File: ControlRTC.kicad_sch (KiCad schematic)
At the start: 36 parts, among them M1 Fan_4pin, SW1 SW_USER, SW2 SW_WIPE, U18 74LVC1G07, U19 74LVC1G07, U20 LP5569RTWR, U21 PCF85063AT, U25 PCF8563TS, Y2 X32K768S301

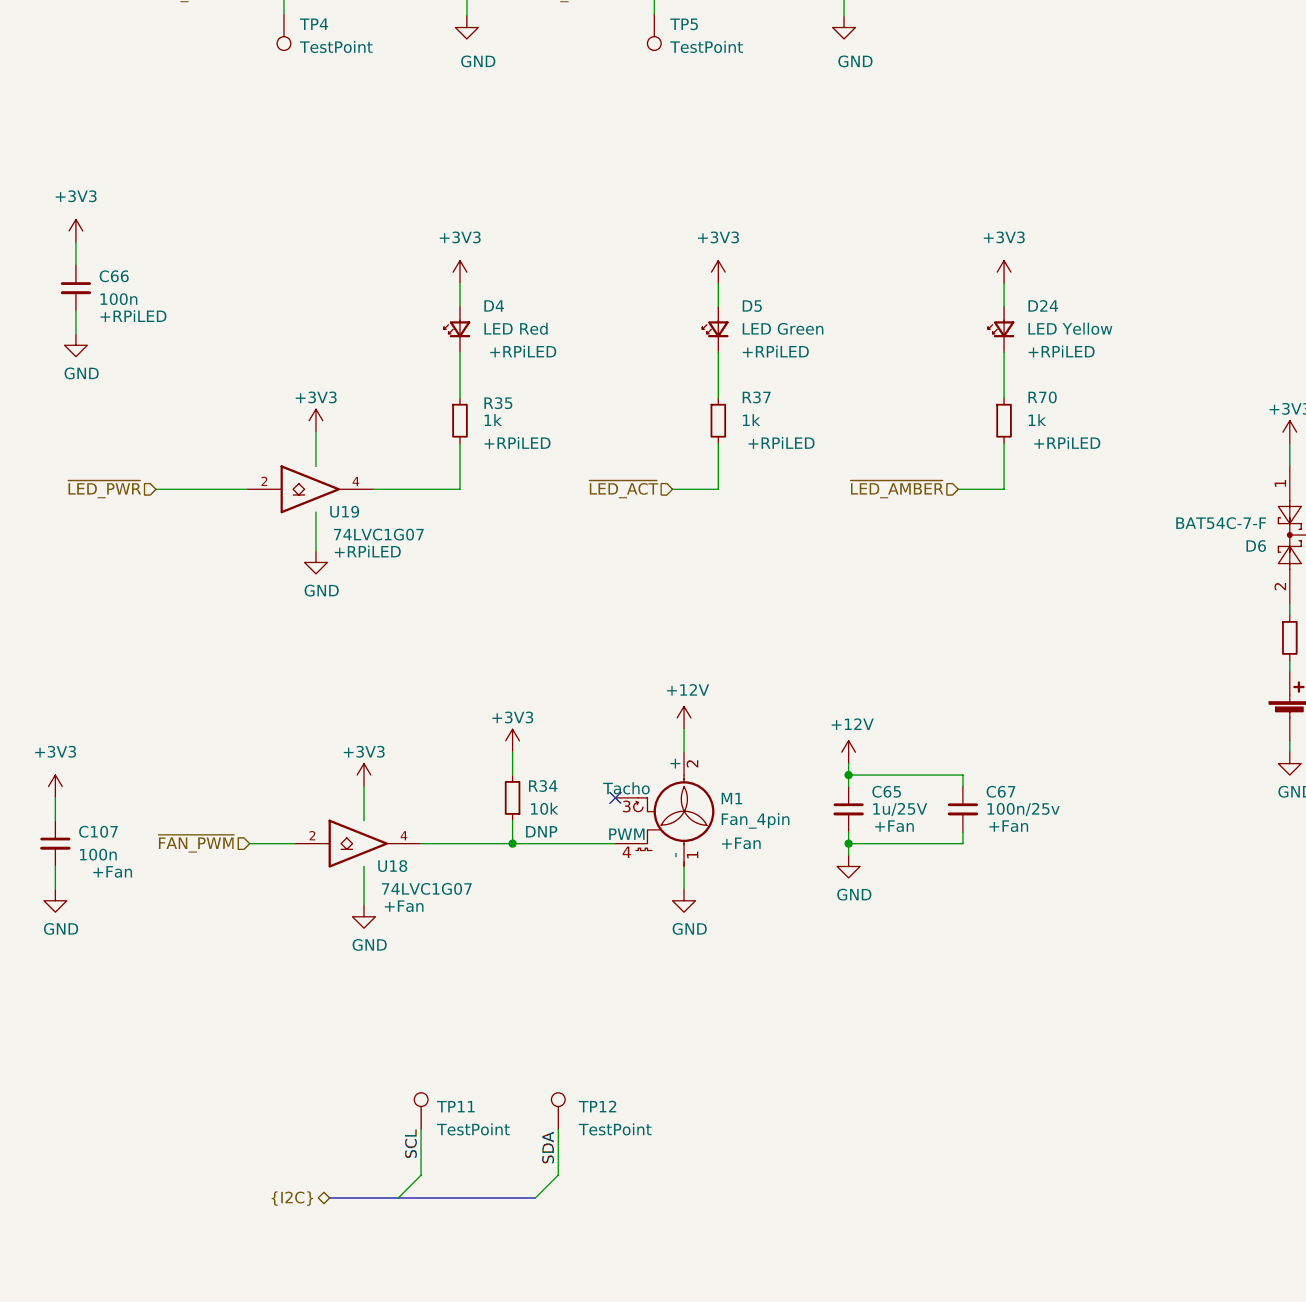
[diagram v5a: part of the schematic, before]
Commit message: Update to LEDs and add GND test point
- Add Blue Radio LED (in a separate new assembly option)
- Change buffer package from SC-70 to SC-74A (aka. SOT-23-5)
- Add GND test point

Fixes: #31

Signed-off-by: Stefan Agner <stefan@agner.ch>
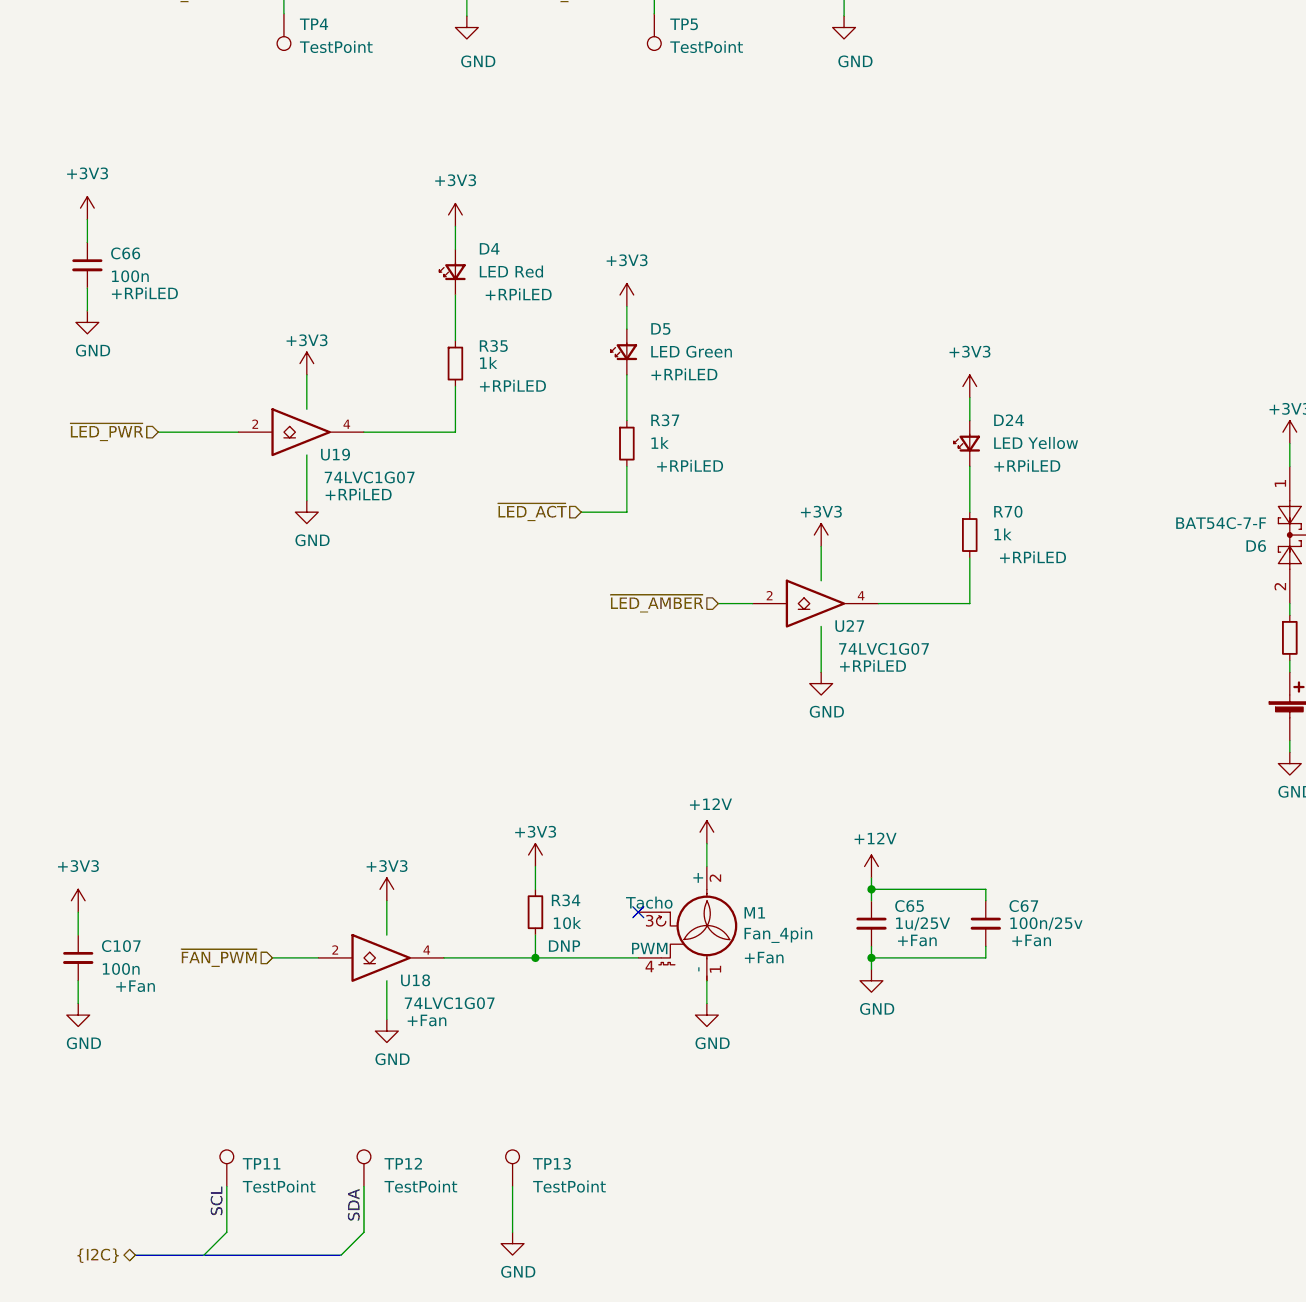
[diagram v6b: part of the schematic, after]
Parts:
- added TP13: TestPoint, TestPoint:TestPoint_Pad_D1.0mm, symbol Connector:TestPoint
- added U27: 74LVC1G07, Package_TO_SOT_SMD:SOT-23-5, symbol 74xGxx:74LVC1G07
- U18, U19: footprint Package_TO_SOT_SMD:SOT-353_SC-70-5 -> Package_TO_SOT_SMD:SOT-23-5; Manufacturer NXP USA -> Texas Instruments; PartNumber 74LVC1G07GW -> SN74LVC1G07DBV
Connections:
- net +3V3: now also U27.5 (VCC)
- net GND: now also TP13.1, U27.3 (GND)
- net ~{LED_AMBER}: now also U27.2; no longer R70.2
- new net: R70.2, U27.4
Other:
- moved on the sheet: C107, C65, C66, C67, D24, D4, D5, M1, R34, R35, R37, R70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

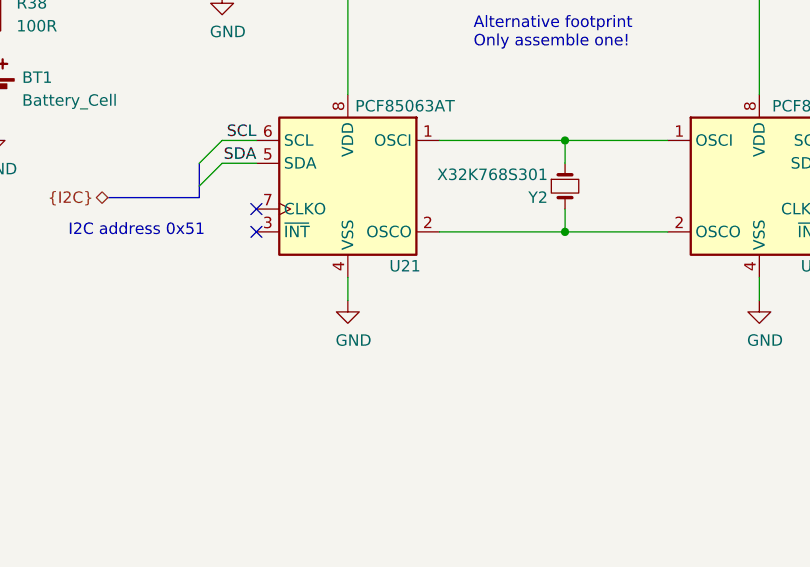
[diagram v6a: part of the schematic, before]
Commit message: Relayout new design
- Update PCB from Schematics
- Move SD-card to bottom side of the PCB
- Place LEDs in front of CM4
- Add additional LEDs (Amber/Radio)
- Move LP5569 to the left
- Remove all holes
- Lock through holes which should not be moved

Fixes: #33

Signed-off-by: Stefan Agner <stefan@agner.ch>
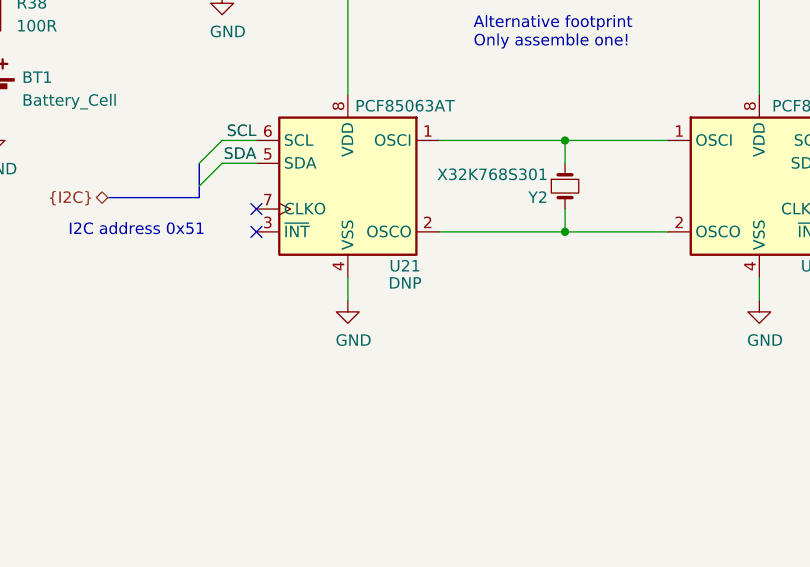
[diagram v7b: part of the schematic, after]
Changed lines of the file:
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@@
       (effects (font (size 1.27 1.27)) hide)
     )
-    (property "Config" "DNP" (id 6) (at 198.12 137.16 0)
-      (effects (font (size 1.27 1.27)) hide)
-    )
+    (property "Config" "DNP" (id 6) (at 204.47 147.955 0))
     (pin "1")
     (pin "2")

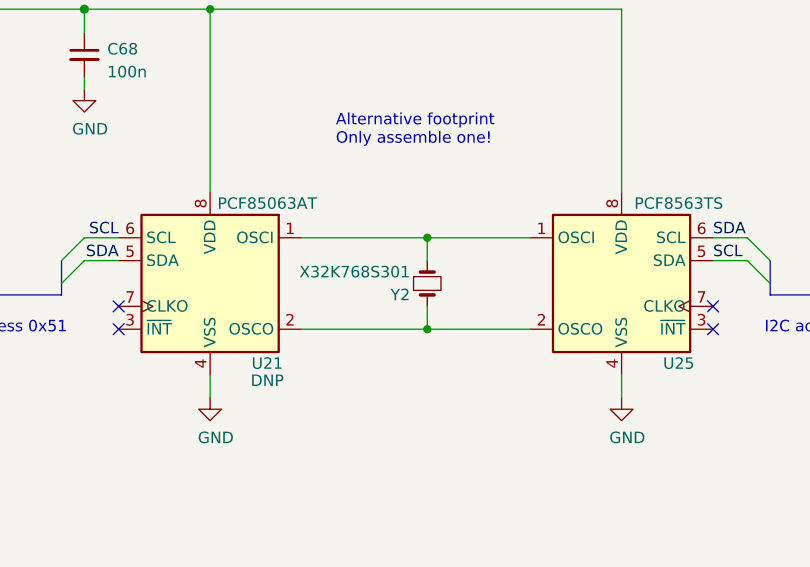
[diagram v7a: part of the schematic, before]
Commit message: Fix/improve various parts
- U7: Define Manufacturer/PartNumber
- J13: Define Manufacturer/PartNumber
- L2: Fix PartNumber (remove unprintable characters)
- C85: Change to our preferred supplier Nichicon
- J9: DNP (not used by default, avoid potential issues with FCC approval)
- Y1/Y2: Define frequency and load capacitance in value
- JP1: Use sensible part value
- C106: Fix Config field
- Remove heat sink and CM4 from BOM (handled in product assembly BOM)

Signed-off-by: Stefan Agner <stefan@agner.ch>
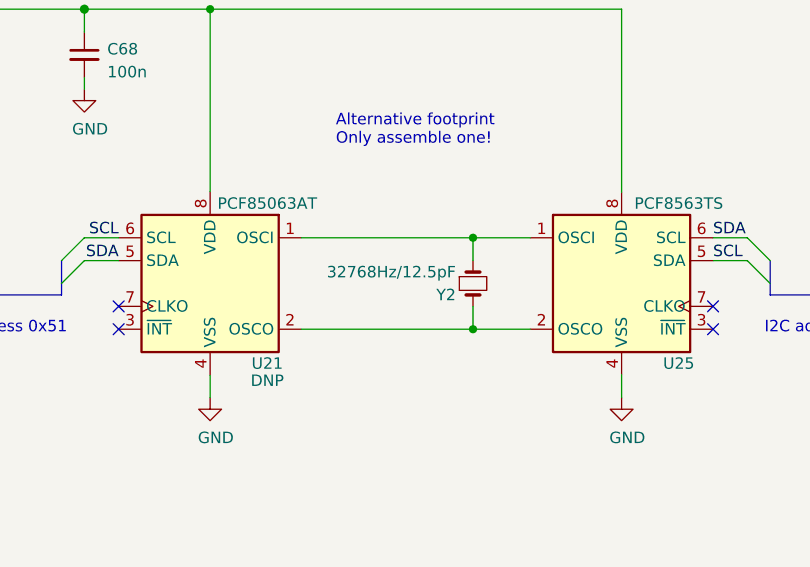
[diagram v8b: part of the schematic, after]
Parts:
- Y2: value X32K768S301 -> 32768Hz/12.5pF; Manufacturer Epson -> Yangxing Tech; PartNumber FC-135 32.7680KA-A3 -> X321532768KGD2SI
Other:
- moved on the sheet: Y2
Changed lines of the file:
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@@
   (junction (at 191.77 76.2) (diameter 0.9144) (color 0 0 0 0))
   (junction (at 198.12 106.68) (diameter 0.9144) (color 0 0 0 0))
-  (junction (at 222.25 132.08) (diameter 0.9144) (color 0 0 0 0))
-  (junction (at 222.25 142.24) (diameter 0.9144) (color 0 0 0 0))
+  (junction (at 227.33 132.08) (diameter 0.9144) (color 0 0 0 0))
+  (junction (at 227.33 142.24) (diameter 0.9144) (color 0 0 0 0))
   (junction (at 238.76 48.26) (diameter 0.9144) (color 0 0 0 0))
   (junction (at 261.62 35.56) (diameter 0.9144) (color 0 0 0 0))
@@
     (stroke (width 0) (type solid) (color 0 0 0 0))
   )
-  (wire (pts (xy 208.28 132.08) (xy 222.25 132.08))
-    (stroke (width 0) (type solid) (color 0 0 0 0))
-  )
-  (wire (pts (xy 208.28 142.24) (xy 222.25 142.24))
+  (wire (pts (xy 208.28 132.08) (xy 227.33 132.08))
+    (stroke (width 0) (type solid) (color 0 0 0 0))
+  )
+  (wire (pts (xy 208.28 142.24) (xy 227.33 142.24))
     (stroke (width 0) (type solid) (color 0 0 0 0))
   )
@@
     (stroke (width 0) (type solid) (color 0 0 0 0))
   )
-  (wire (pts (xy 222.25 132.08) (xy 233.68 132.08))
-    (stroke (width 0) (type solid) (color 0 0 0 0))
-  )
-  (wire (pts (xy 222.25 134.62) (xy 222.25 132.08))
-    (stroke (width 0) (type solid) (color 0 0 0 0))
-  )
-  (wire (pts (xy 222.25 139.7) (xy 222.25 142.24))
-    (stroke (width 0) (type solid) (color 0 0 0 0))
-  )
-  (wire (pts (xy 222.25 142.24) (xy 233.68 142.24))
-    (stroke (width 0) (type solid) (color 0 0 0 0))
-  )
   (wire (pts (xy 223.52 43.18) (xy 226.06 43.18))
     (stroke (width 0) (type solid) (color 0 0 0 0))
@@
   )
   (wire (pts (xy 224.79 34.29) (xy 224.79 36.83))
+    (stroke (width 0) (type solid) (color 0 0 0 0))
+  )
+  (wire (pts (xy 227.33 132.08) (xy 233.68 132.08))
+    (stroke (width 0) (type solid) (color 0 0 0 0))
+  )
+  (wire (pts (xy 227.33 134.62) (xy 227.33 132.08))
+    (stroke (width 0) (type solid) (color 0 0 0 0))
+  )
+  (wire (pts (xy 227.33 139.7) (xy 227.33 142.24))
+    (stroke (width 0) (type solid) (color 0 0 0 0))
+  )
+  (wire (pts (xy 227.33 142.24) (xy 233.68 142.24))
     (stroke (width 0) (type solid) (color 0 0 0 0))
   )
@@
     (pin "2")
   )
-  (symbol (lib_id "Device:Crystal_Small") (at 222.25 137.16 270) (unit 1)
-    (in_bom yes) (on_board yes)
-    (property "Reference" "Y2" (id 0) (at 220.345 138.43 90)
+  (symbol (lib_id "Device:Crystal_Small") (at 227.33 137.16 270) (unit 1)
+    (in_bom yes) (on_board yes)
+    (property "Reference" "Y2" (id 0) (at 225.425 138.43 90)
       (effects (font (size 1.27 1.27)) (justify right))
     )
-    (property "Value" "X32K768S301" (id 1) (at 220.345 135.89 90)
+    (property "Value" "32768Hz{slash}12.5pF" (id 1) (at 225.425 135.89 90)
       (effects (font (size 1.27 1.27)) (justify right))
     )
-    (property "Footprint" "Crystal:Crystal_SMD_3215-2Pin_3.2x1.5mm" (id 2) (at 222.25 137.16 0)
-      (effects (font (size 1.27 1.27)) hide)
-    )
-    (property "Datasheet" "~" (id 3) (at 222.25 137.16 0)
-      (effects (font (size 1.27 1.27)) hide)
-    )
-    (property "Manufacturer" "Epson" (id 4) (at 222.25 137.16 0)
-      (effects (font (size 1.27 1.27)) hide)
-    )
-    (property "PartNumber" "FC-135 32.7680KA-A3" (id 5) (at 222.25 137.16 0)
-      (effects (font (size 1.27 1.27)) hide)
-    )
+    (property "Footprint" "Crystal:Crystal_SMD_3215-2Pin_3.2x1.5mm" (id 2) (at 227.33 137.16 0)
+      (effects (font (size 1.27 1.27)) hide)
+    )
+    (property "Datasheet" "~" (id 3) (at 227.33 137.16 0)
+      (effects (font (size 1.27 1.27)) hide)
+    )
+    (property "Manufacturer" "Yangxing Tech" (id 4) (at 227.33 137.16 0)
+      (effects (font (size 1.27 1.27)) hide)
+    )
+    (property "PartNumber" "X321532768KGD2SI" (id 5) (at 227.33 137.16 0)
+      (effects (font (size 1.27 1.27)) hide)
+    )
